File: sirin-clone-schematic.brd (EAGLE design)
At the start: 101.6 x 55.9 mm, 21 parts

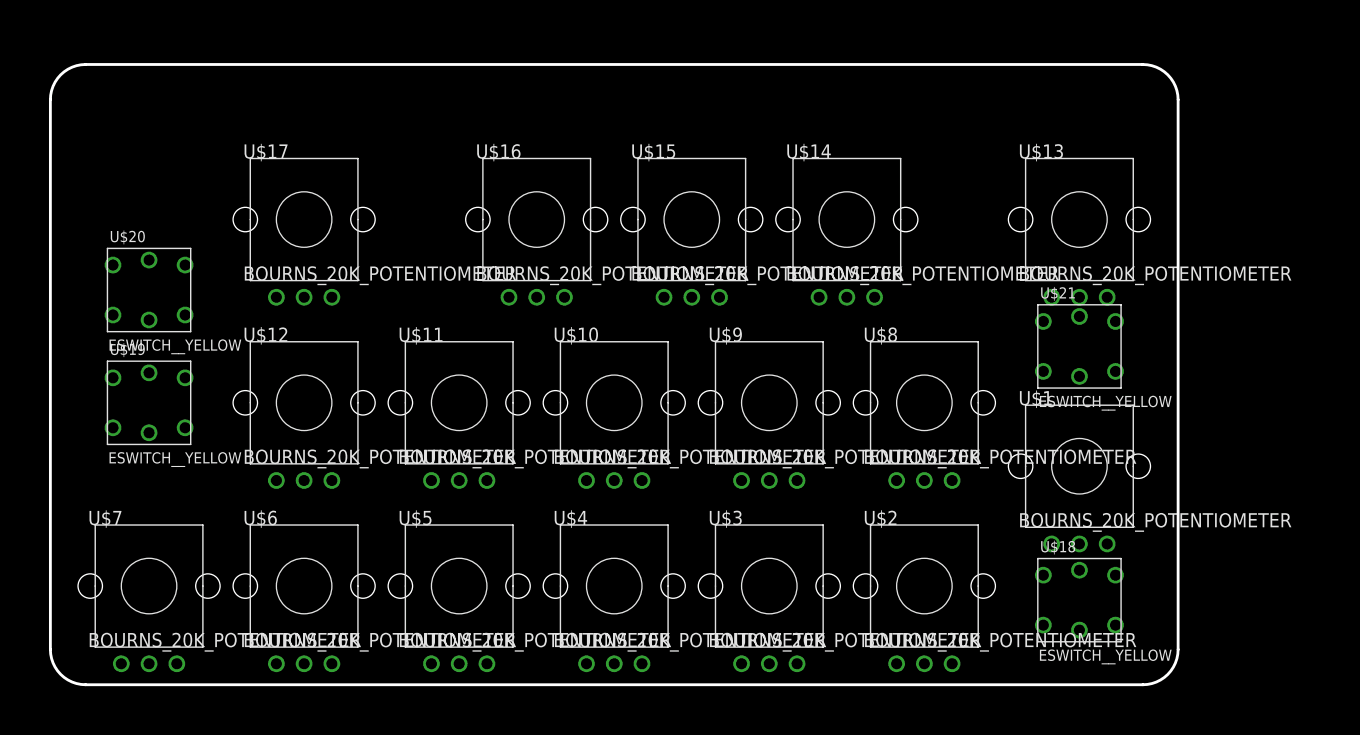
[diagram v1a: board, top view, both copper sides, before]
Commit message: add midi
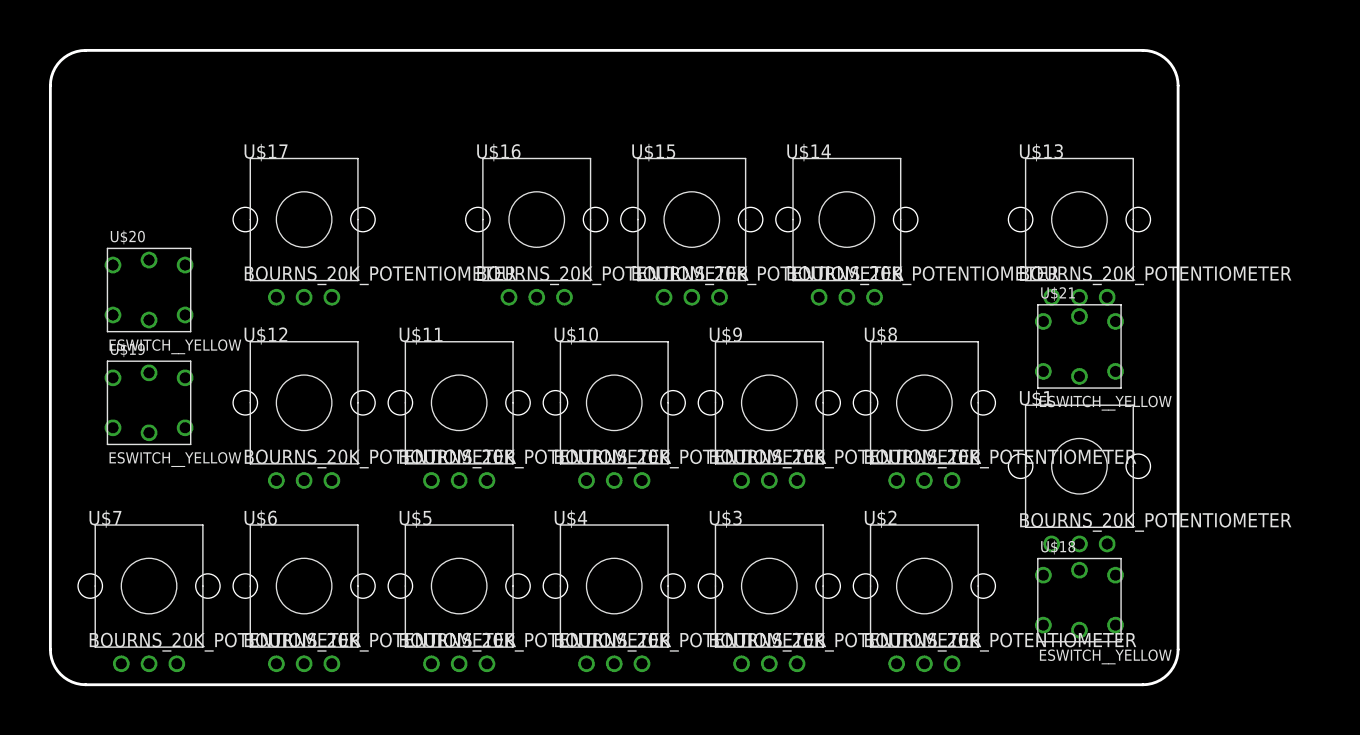
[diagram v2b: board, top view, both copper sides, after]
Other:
- board size 101.6 x 55.9 mm -> 101.6 x 57.1 mm
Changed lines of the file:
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@@
 <setting verticaltext="up"/>
 </settings>
-<grid distance="50" unitdist="mil" unit="mil" style="lines" multiple="1" display="yes" altdistance="5" altunitdist="mil" altunit="mil"/>
+<grid distance="50" unitdist="mil" unit="inch" style="lines" multiple="1" display="yes" altdistance="5" altunitdist="mil" altunit="mil"/>
 <layers>
 <layer number="1" name="Top" color="4" fill="1" visible="yes" active="yes"/>
@@
 </layers>
 <board>
-<fusionsync huburn="a.cGVyc29uYWw6dWUyOWViOTli" projecturn="a.cGVyc29uYWw6dWUyOWViOTliIzIwMTkwMjI4MTc5MjYyNDAx" f3durn="urn:adsk.wipprod:dm.lineage:6XGW8_IMTfahicU4G-4h1g" pcbguid="68cec704-b38b-4bc9-8c00-2951139b60a6" lastpulledtime="2019-02-28T14:47:30Z" lastsyncedchangeguid="3a167f73-e2ae-04cd-7bee-3db2df5f0cc5"/>
+<fusionsync huburn="a.cGVyc29uYWw6dWUyOWViOTli" projecturn="a.cGVyc29uYWw6dWUyOWViOTliIzIwMTkwMjI4MTc5MjYyNDAx" f3durn="urn:adsk.wipprod:dm.lineage:6XGW8_IMTfahicU4G-4h1g" pcbguid="68cec704-b38b-4bc9-8c00-2951139b60a6" lastpulledtime="2019-03-13T20:54:59Z" lastsyncedchangeguid="81379807-6f50-57a2-7027-f1975fa9e0e9"/>
 <plain>
 <wire x1="0" y1="3.175" x2="3.175" y2="0" width="0.254" layer="20" curve="90"/>
 <wire x1="3.175" y1="0" x2="98.425" y2="0" width="0.254" layer="20"/>
 <wire x1="98.425" y1="0" x2="101.6" y2="3.175" width="0.254" layer="20" curve="90"/>
-<wire x1="101.6" y1="3.175" x2="101.6" y2="52.705" width="0.254" layer="20"/>
-<wire x1="101.6" y1="52.705" x2="98.425" y2="55.88" width="0.254" layer="20" curve="90"/>
-<wire x1="98.425" y1="55.88" x2="3.175" y2="55.88" width="0.254" layer="20"/>
-<wire x1="3.175" y1="55.88" x2="0" y2="52.705" width="0.254" layer="20" curve="90"/>
-<wire x1="0" y1="52.705" x2="0" y2="3.175" width="0.254" layer="20"/>
+<wire x1="101.6" y1="3.175" x2="101.6" y2="53.975" width="0.254" layer="20"/>
+<wire x1="101.6" y1="53.975" x2="98.425" y2="57.15" width="0.254" layer="20" curve="90"/>
+<wire x1="98.425" y1="57.15" x2="3.175" y2="57.15" width="0.254" layer="20"/>
+<wire x1="3.175" y1="57.15" x2="0" y2="53.975" width="0.254" layer="20" curve="90"/>
+<wire x1="0" y1="53.975" x2="0" y2="3.175" width="0.254" layer="20"/>
 </plain>
 <attributes>

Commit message: lots o' routing
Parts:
- removed U$11: BOURNS_20K_POTENTIOMETER, sirin-clone-library:BOURNS_PTV09
- added J1: 30_PIN_CONNECTOR_MALE, sirin-clone-library:MOLEX_30PINCONNECTOR_2MM
- added R1, R2, R3, R4: 75OHM, sirin-clone-library:0805
- moved U$8 57.9 mm to (22.9, 40.6), turned to 180 degrees
- moved U$14 52.0 mm to (22.9, 24.1), turned to 180 degrees
- moved U$3 42.3 mm to (92.7, 40.6), turned to 180 degrees
- moved U$15 42.1 mm to (92.7, 18.4), turned to 180 degrees
- moved U$5 41.9 mm to (78.7, 7.62), turned to 180 degrees
- moved U$1 39.6 mm to (59.1, 40.6), turned to 180 degrees
- moved U$12 36.2 mm to (59.1, 24.1), turned to 180 degrees
- moved U$16 35.0 mm to (36.8, 7.62), turned to 180 degrees
- moved U$10 29.1 mm to (75.6, 40.6), turned to 180 degrees
- moved U$2 28.0 mm to (50.8, 7.62), turned to 180 degrees
- moved U$9 26.9 mm to (42.5, 40.6), turned to 180 degrees
- moved U$17 26.5 mm to (42.5, 24.1), turned to 180 degrees
- moved U$13 24.7 mm to (75.6, 24.1), turned to 180 degrees
- moved U$4 14.0 mm to (64.8, 7.62), turned to 180 degrees
- moved U$20 5.08 mm to (8.89, 40.6)
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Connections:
- new net 3.3V: J1.P$14, J1.P$15, U$1.1, U$10.1, U$12.1, U$13.1, U$14.1, U$15.1, U$16.1, U$17.1, U$2.1, U$3.1, U$4.1, U$5.1, U$6.1, U$7.1, U$8.1, U$9.1
- new net GND: J1.P$29, J1.P$30, U$1.3, U$10.3, U$12.3, U$13.3, U$14.3, U$15.3, U$16.3, U$17.3, U$18.-, U$18.1, U$18.2, U$19.-, U$19.1, U$19.2, U$2.3, U$20.-, U$20.1, U$20.2, U$21.-, U$21.1, U$21.2, U$3.3, U$4.3, U$5.3, U$6.3, U$7.3, U$8.3, U$9.3
- new net N$1: R1.1, U$18.+
- new net N$2: R2.1, U$19.+
- new net N$3: R3.1, U$20.+
- new net N$4: R4.1, U$21.+
- new net PIN15/KNOB1(VOL): J1.P$24, U$13.2
- new net PIN16/KNOB2: J1.P$28, U$6.2
- new net PIN17/KNOB3: J1.P$27, U$7.2
- new net PIN2/SW1: J1.P$19, U$18.3, U$18.4
- new net PIN20/KNOB4: J1.P$4, U$8.2
- new net PIN21/KNOB5: J1.P$5, U$9.2
- new net PIN24/LED1: J1.P$16, R1.2
- new net PIN25/LED2: J1.P$25, R2.2
- new net PIN26/KNOB6: J1.P$9, U$10.2
- new net PIN27/KNOB7: J1.P$22, U$17.2
- new net PIN28/KNOB8: J1.P$23, U$12.2
- new net PIN29/KNOB9: J1.P$21, U$14.2
- new net PIN3/SW2: J1.P$17, U$19.3, U$19.4
- new net PIN30/KNOB10: J1.P$20, U$15.2
- new net PIN31/KNOB11: J1.P$8, U$1.2
- new net PIN32/LED3: J1.P$26, R3.2
- new net PIN33/LED4: J1.P$1, R4.2
- new net PIN4/SW3: J1.P$18, U$20.3, U$20.4
- new net PIN5/SW4: J1.P$6, U$21.3, U$21.4
- new net PIN8/MIDILED: J1.P$3
- new net PINA10/KNOB12: J1.P$11, U$2.2
- new net PINA11/KNOB13: J1.P$10, U$3.2
- new net PINA12/KNOB14: J1.P$12, U$4.2
- new net PINA13/KNOB15: J1.P$13, U$5.2
- new net PINA14/KNOB16: J1.P$7, U$16.2
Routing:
- net 3.3V: track 0.00 -> 412.9 mm
- net PIN17/KNOB3: track 0.00 -> 117.0 mm
- net PIN25/LED2: track 0.00 -> 94.4 mm, vias 0 -> 9
- net PIN32/LED3: track 0.00 -> 92.7 mm, vias 0 -> 5
- net PIN16/KNOB2: track 0.00 -> 91.1 mm, vias 0 -> 7
- net PIN2/SW1: track 0.00 -> 89.1 mm, vias 0 -> 9
- net PIN3/SW2: track 0.00 -> 88.2 mm, vias 0 -> 6
- net PIN24/LED1: track 0.00 -> 88.0 mm, vias 0 -> 12
- net PIN4/SW3: track 0.00 -> 75.8 mm, vias 0 -> 4
- net PINA14/KNOB16: track 0.00 -> 74.0 mm, vias 0 -> 6
- net PINA10/KNOB12: track 0.00 -> 71.4 mm, vias 0 -> 4
- net PIN33/LED4: track 0.00 -> 70.3 mm, vias 0 -> 5
- net PIN29/KNOB9: track 0.00 -> 67.4 mm, vias 0 -> 2
- net PINA12/KNOB14: track 0.00 -> 58.4 mm, vias 0 -> 4
- net PIN27/KNOB7: track 0.00 -> 57.1 mm, vias 0 -> 2
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- added copper zone on layer 16, net GND

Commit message: ready for gerbers
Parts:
- added D1: (no value), sirin-clone-library:CHIPLED_0805
- added R5: 75OHM, sirin-clone-library:0805
- moved R4 0.90 mm to (98.2, 30.2)
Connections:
- new net AGND: J1.P$29, J1.P$30, U$1.3, U$10.3, U$12.3, U$13.3, U$14.3, U$15.3, U$16.3, U$17.3, U$2.3, U$3.3, U$4.3, U$5.3, U$6.3, U$7.3, U$8.3, U$9.3
- new net N$6: D1.A, R5.1
- net GND: now also D1.C, J1.P$13; no longer J1.P$29, J1.P$30, U$1.3, U$10.3, U$12.3, U$13.3, U$14.3, U$15.3, U$16.3, U$17.3, U$2.3, U$3.3, U$4.3, U$5.3, U$6.3, U$7.3, U$8.3, U$9.3
- net PIN20/KNOB4: now also J1.P$3; no longer J1.P$4
- net PIN21/KNOB5: now also J1.P$4; no longer J1.P$5
- net PIN26/KNOB6: now also J1.P$8; no longer J1.P$9
- net PIN31/KNOB11: now also J1.P$7; no longer J1.P$8
- net PIN5/SW4: now also J1.P$5; no longer J1.P$6
- net PIN8/MIDILED: now also J1.P$2, R5.2; no longer J1.P$3
- net PINA10/KNOB12: now also J1.P$10; no longer J1.P$11
- net PINA11/KNOB13: now also J1.P$9; no longer J1.P$10
- net PINA12/KNOB14: now also J1.P$11; no longer J1.P$12
- net PINA13/KNOB15: now also J1.P$12; no longer J1.P$13
- net PINA14/KNOB16: now also J1.P$6; no longer J1.P$7
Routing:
- net GND: track 0.00 -> 240.7 mm, vias 0 -> 1
- net PIN8/MIDILED: track 0.00 -> 65.5 mm, vias 0 -> 9
- net N$6: track 0.00 -> 3.76 mm
- net PIN5/SW4: track 52.7 -> 54.9 mm
- net PINA13/KNOB15: track 51.0 -> 53.1 mm, vias 4 -> 5
- net PIN21/KNOB5: track 37.3 -> 35.3 mm
- net PINA11/KNOB13: track 13.7 -> 15.7 mm, vias 1 -> 2
- net PIN20/KNOB4: track 53.5 -> 51.6 mm
- net PINA12/KNOB14: track 58.4 -> 60.0 mm
- net PINA10/KNOB12: track 71.4 -> 72.3 mm
- net PIN33/LED4: track 70.3 -> 71.1 mm
- net PIN17/KNOB3: track 117.0 -> 117.2 mm, vias 0 -> 1
- added copper zone on layer 16, net AGND
- removed copper zone on layer 16, net GND
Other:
- board text added: "CONTROL BOARD V0.0.1 MAR 2019 BY K. MARUT"

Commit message: adding bom attributes
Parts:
- U$1, U$10, U$12, U$13, U$14, U$15, U$16, U$17, U$2, U$3, U$4, U$5, U$6, U$7, U$8, U$9: value BOURNS_20K_POTENTIOMETER -> BOURNS_10K_POTENTIOMETER
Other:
- board text added: "3.3V"
- board text added: "AGND"
- board text added: "GND"
- board text added: "PIN1"
- board text added: "PIN16"
